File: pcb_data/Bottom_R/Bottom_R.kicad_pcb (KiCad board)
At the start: 2 copper layers, 186.9 x 96.4 mm, 103 parts, among them J1 Conn_01x02, U1 XIAO-nRF52840

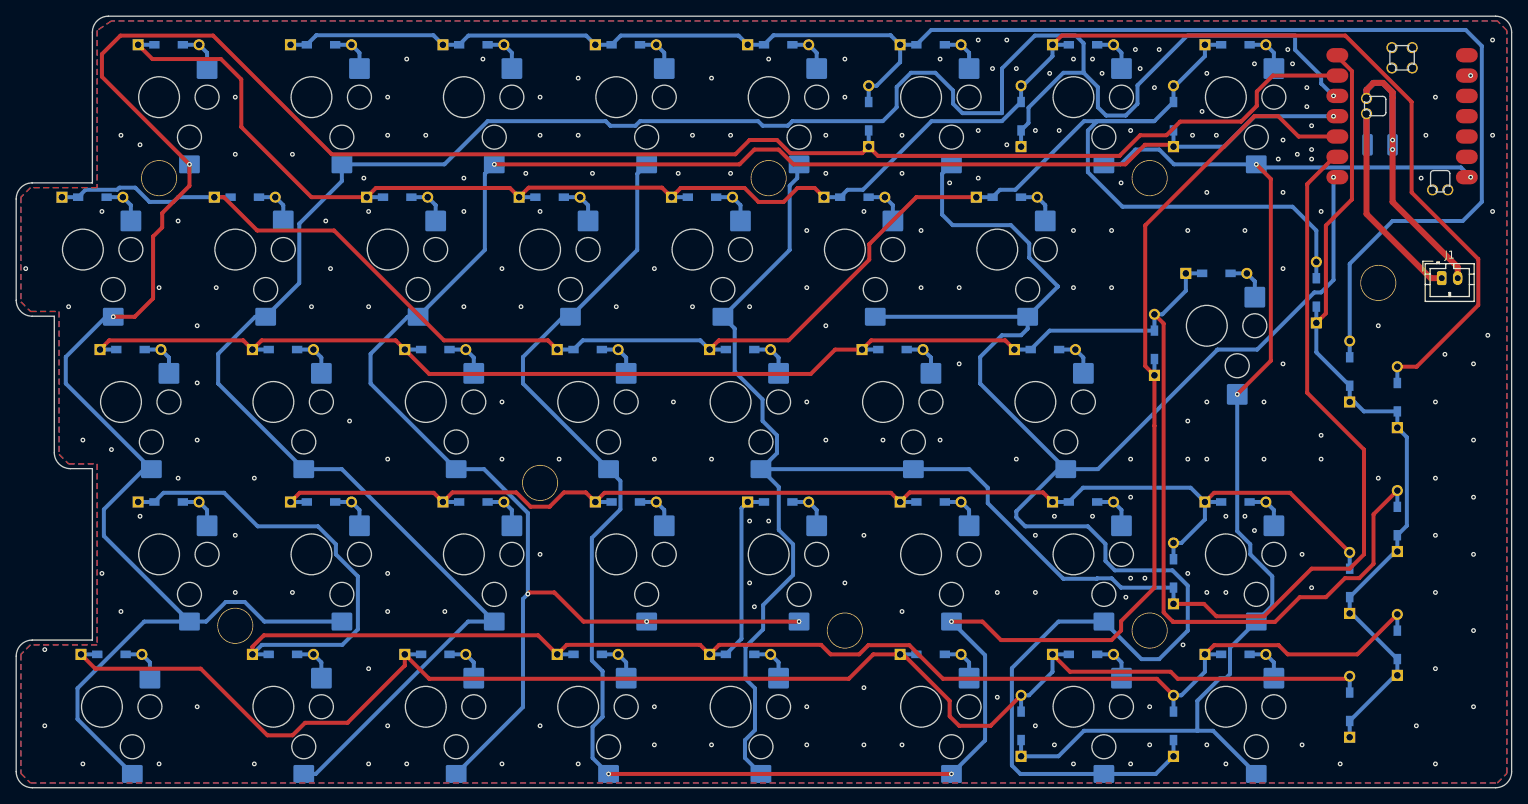
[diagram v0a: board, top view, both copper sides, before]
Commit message: remove unnecessary footprint
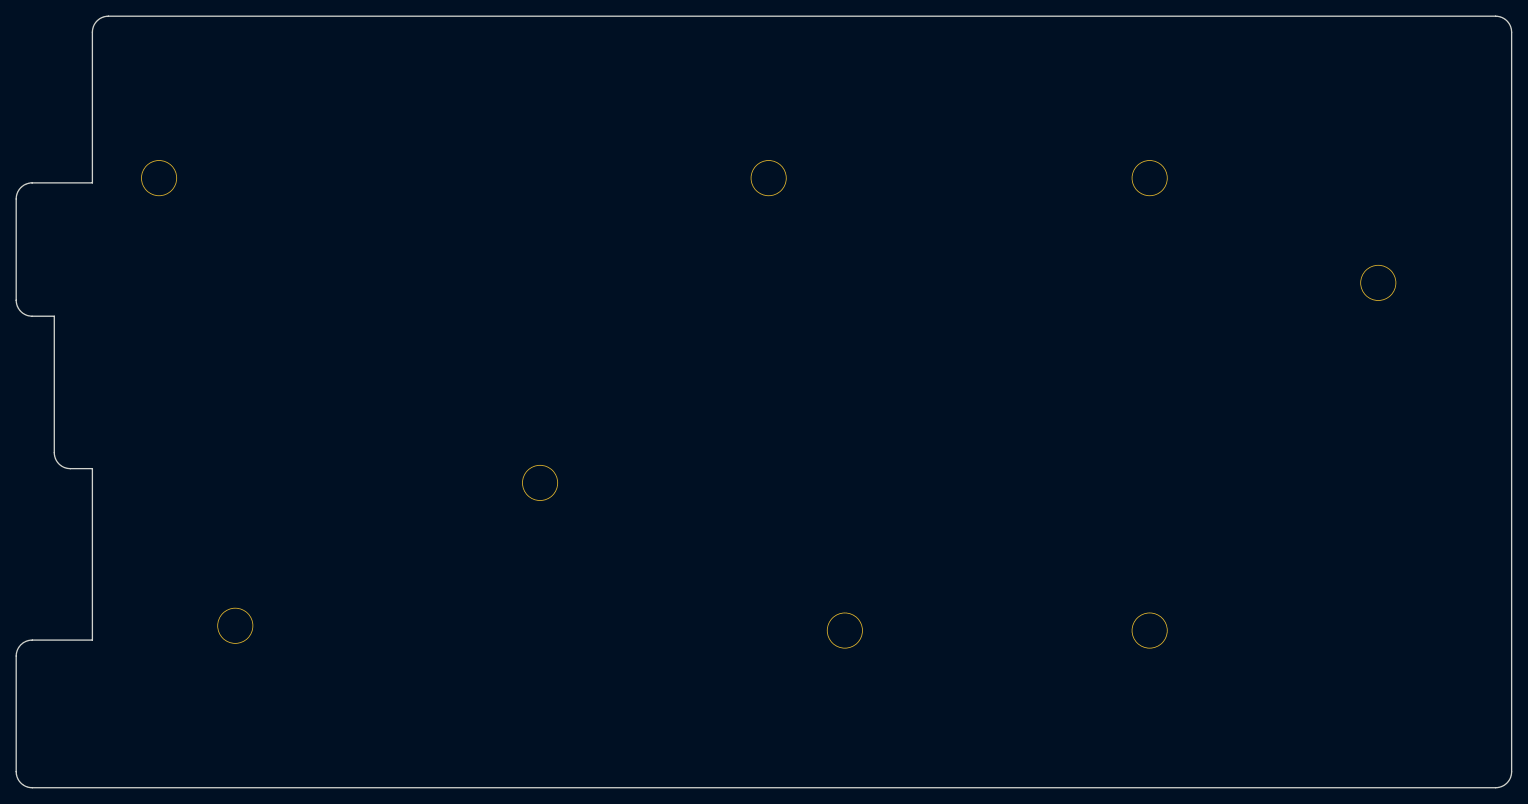
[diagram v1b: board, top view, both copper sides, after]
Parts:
- removed C1: GRM32EC81C476KE15L, Capacitor_SMD:C_1210_3225Metric_Pad1.33x2.70mm_HandSolder
- removed D0-10, D0-11, D0-12, D0-13, D0-8, D0-9, D1-10, D1-11, D1-12, D1-7, D1-9, D2-10, D2-11, D2-12, D2-13, D2-7, D2-8, D3-11, D3-12, D3-13, D3-7, D3-8, D3-9, D4-10, D4-12, D4-7, D4-8, D4-9, D5-10, D5-11, D5-13, D5-7, D5-8, D5-9, D6-10, D6-11, D6-12, D6-8, D6-9, DI10, DI11, DI12, DI13, DI7, DI8, DI9, DS10, DS11, DS12, DS13, DS7, DS8, DS9: 1N4148W, kbd_Parts:Diode_TH_SMD
- removed J1: Conn_01x02, Connector_JST:JST_PH_B2B-PH-K_1x02_P2.00mm_Vertical
- removed RC0-10, RC0-11, RC0-12, RC0-8, RC0-9, RC1-10, RC1-11, RC1-12, RC1-7, RC1-9, RC2-10, RC2-11, RC2-12, RC2-13, RC2-7, RC2-8, RC3-11, RC3-12, RC3-13, RC3-7, RC3-8, RC3-9, RC4-10, RC4-12, RC4-7, RC4-8, RC4-9, RC5-10, RC5-11, RC5-13, RC5-7, RC5-8, RC5-9, RC6-11, RC6-12, RC6-8, RC6-9: SW_Push, custom-library:Kailh-PG1353-Hotswap-R-1U
- removed RC0-13: SW_Push, custom-library:Kailh-PG1353-Hotswap-R-1.25U
- removed RC6-10: SW_Push, custom-library:Kailh-PG1353-Hotswap-ISOEnter-R
- removed U1: XIAO-nRF52840, mcu:xiao-ble-smd-cutout
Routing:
- net IO 7: track 318.6 -> 0.00 mm, vias 2 -> 0
- net IO 8: track 286.5 -> 0.00 mm, vias 1 -> 0
- net IO 10: track 264.8 -> 0.00 mm, vias 3 -> 0
- net Net-(D0-12-K): track 245.6 -> 0.00 mm
- net IO 9: track 243.9 -> 0.00 mm, vias 5 -> 0
- net Net-(D0-8-K): track 243.5 -> 0.00 mm
- net IO 12: track 238.5 -> 0.00 mm, vias 1 -> 0
- net Net-(D0-10-K): track 237.6 -> 0.00 mm
- net IO 11: track 232.4 -> 0.00 mm
- net Net-(D0-9-K): track 229.8 -> 0.00 mm
- net Net-(D1-7-K): track 214.6 -> 0.00 mm
- net Net-(D0-13-K): track 193.7 -> 0.00 mm
- net Net-(D0-11-K): track 164.4 -> 0.00 mm
- net IO 13: track 162.5 -> 0.00 mm, vias 3 -> 0
- net INTR_R: track 106.3 -> 0.00 mm
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- removed copper zone on B.Cu, net GND
- removed copper zone on F.Cu, net GND

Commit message: fix hole footprint and number
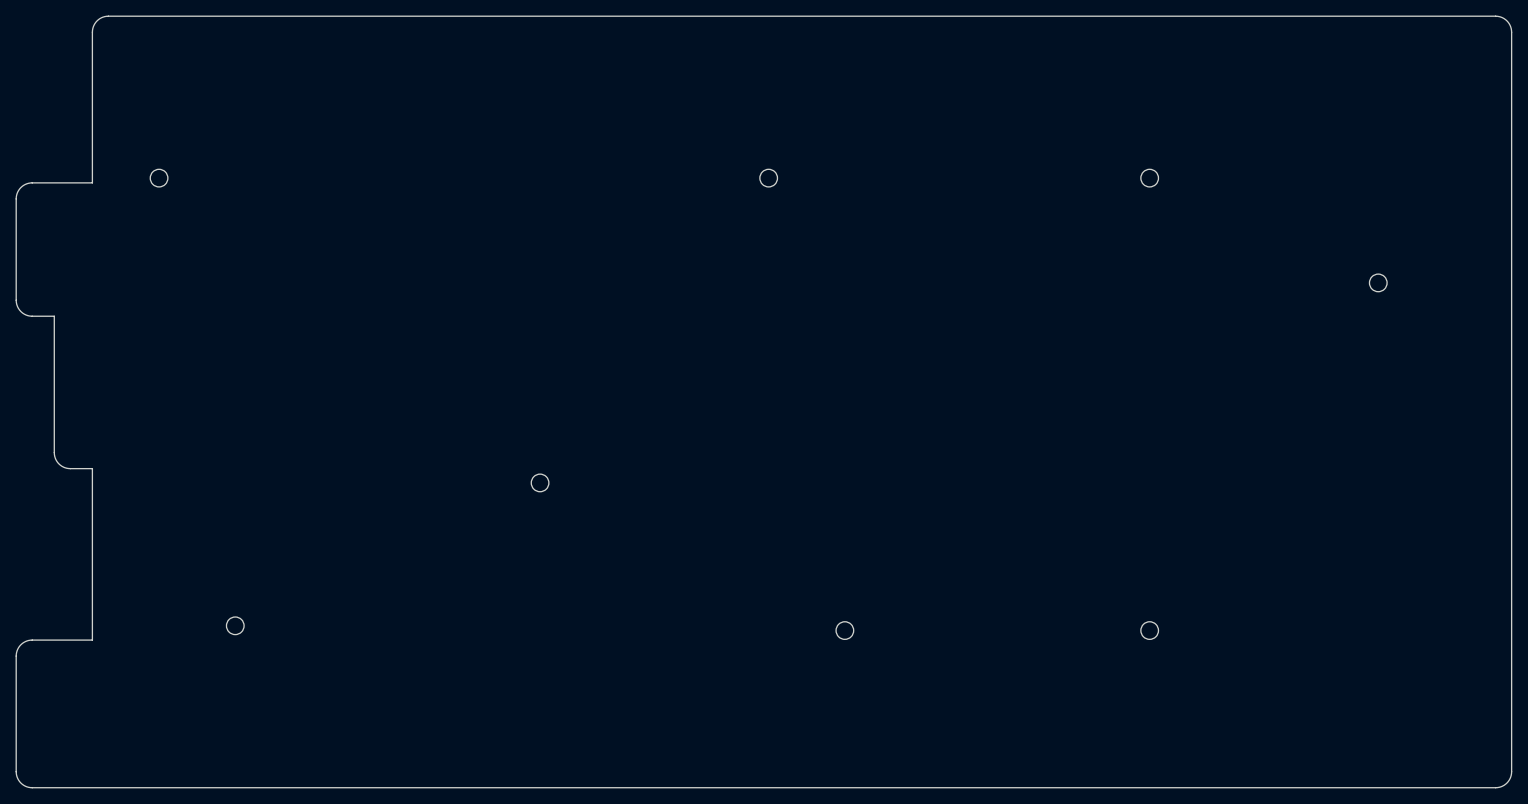
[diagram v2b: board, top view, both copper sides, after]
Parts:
- H1, H2, H3, H4, H5, H6: footprint kbd_Hole:m2_Spacer_Hole -> kbd_Hole:m2_Screw_Hole
- H7: renamed from H8; footprint kbd_Hole:m2_Spacer_Hole -> kbd_Hole:m2_Screw_Hole
- H8: renamed from H7; footprint kbd_Hole:m2_Spacer_Hole -> kbd_Hole:m2_Screw_Hole
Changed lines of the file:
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@@
 	)
 	(net 0 "")
-	(footprint "kbd_Hole:m2_Spacer_Hole"
+	(footprint "kbd_Hole:m2_Screw_Hole"
 		(layer "F.Cu")
 		(at 207.168924 67.270369)
@@
 			)
 		)
-		(property "Datasheet" "~"
-			(at 0 0 0)
-			(layer "F.Fab")
-			(hide yes)
-			(effects
-				(font
-					(size 1.27 1.27)
-					(thickness 0.15)
-				)
-			)
-		)
-		(property "Description" "Mounting Hole without connection"
+		(property "Datasheet" ""
+			(at 0 0 0)
+			(layer "F.Fab")
+			(hide yes)
+			(effects
+				(font
+					(size 1.27 1.27)
+					(thickness 0.15)
+				)
+			)
+		)
+		(property "Description" ""
 			(at 0 0 0)
 			(layer "F.Fab")
@@
 		(fp_circle
 			(center 0 0)
-			(end 2.3 0)
+			(end 2.45 0)
 			(stroke
 				(width 0.05)
@@
 		(pad "" np_thru_hole circle
 			(at 0 0)
-			(size 4.5 4.5)
-			(drill 4.3)
+			(size 2.2 2.2)
+			(drill 2.2)
 			(layers "*.Cu" "*.Mask")
 		)
 		(embedded_fonts no)
 	)
-	(footprint "kbd_Hole:m2_Spacer_Hole"
+	(footprint "kbd_Hole:m2_Screw_Hole"
 		(layer "F.Cu")
 		(at 207.168924 123.825104)
@@
 			)
 		)
-		(property "Datasheet" "~"
-			(at 0 0 0)
-			(layer "F.Fab")
-			(hide yes)
-			(effects
-				(font
-					(size 1.27 1.27)
-					(thickness 0.15)
-				)
-			)
-		)
-		(property "Description" "Mounting Hole without connection"
+		(property "Datasheet" ""
+			(at 0 0 0)
+			(layer "F.Fab")
+			(hide yes)
+			(effects
+				(font
+					(size 1.27 1.27)
+					(thickness 0.15)
+				)
+			)
+		)
+		(property "Description" ""
 			(at 0 0 0)
 			(layer "F.Fab")
@@
 		(fp_circle
 			(center 0 0)
-			(end 2.3 0)
+			(end 2.45 0)
 			(stroke
 				(width 0.05)
@@
 		(pad "" np_thru_hole circle
 			(at 0 0)
-			(size 4.5 4.5)
-			(drill 4.3)
+			(size 2.2 2.2)
+			(drill 2.2)
 			(layers "*.Cu" "*.Mask")
 		)
 		(embedded_fonts no)
 	)
-	(footprint "kbd_Hole:m2_Spacer_Hole"
+	(footprint "kbd_Hole:m2_Screw_Hole"
 		(layer "F.Cu")
 		(at 235.743948 80.367255)
 		(descr "Mounting Hole 2.2mm, no annular, M2")
 		(tags "mounting hole 2.2mm no annular m2")
-		(property "Reference" "H7"
+		(property "Reference" "H8"
 			(at 0 -3.2 0)
 			(layer "F.Fab")
@@
 			)
 		)
-		(property "Datasheet" "~"
-			(at 0 0 0)
-			(layer "F.Fab")
-			(hide yes)
-			(effects
-				(font
-					(size 1.27 1.27)
-					(thickness 0.15)
-				)
-			)
-		)
-		(property "Description" "Mounting Hole without connection"
+		(property "Datasheet" ""
+			(at 0 0 0)
+			(layer "F.Fab")
+			(hide yes)
+			(effects
+				(font
+					(size 1.27 1.27)
+					(thickness 0.15)
+				)
+			)
+		)
+		(property "Description" ""
 			(at 0 0 0)
 			(layer "F.Fab")
@@
 		(fp_circle
 			(center 0 0)
-			(end 2.3 0)
+			(end 2.45 0)
 			(stroke
 				(width 0.05)
@@
 		(pad "" np_thru_hole circle
 			(at 0 0)
-			(size 4.5 4.5)
-			(drill 4.3)
+			(size 2.2 2.2)
+			(drill 2.2)
 			(layers "*.Cu" "*.Mask")
 		)
 		(embedded_fonts no)
 	)
-	(footprint "kbd_Hole:m2_Spacer_Hole"
+	(footprint "kbd_Hole:m2_Screw_Hole"
 		(layer "F.Cu")
 		(at 130.96886 105.370401)
 		(descr "Mounting Hole 2.2mm, no annular, M2")
 		(tags "mounting hole 2.2mm no annular m2")
-		(property "Reference" "H8"
+		(property "Reference" "H7"
 			(at 0 -3.2 0)
 			(layer "F.Fab")
@@
 			)
 		)
-		(property "Datasheet" "~"
-			(at 0 0 0)
-			(layer "F.Fab")
-			(hide yes)
-			(effects
-				(font
-					(size 1.27 1.27)
-					(thickness 0.15)
-				)
-			)
-		)
-		(property "Description" "Mounting Hole without connection"
+		(property "Datasheet" ""
+			(at 0 0 0)
+			(layer "F.Fab")
+			(hide yes)
+			(effects
+				(font
+					(size 1.27 1.27)
+					(thickness 0.15)
+				)
+			)
+		)
+		(property "Description" ""
 			(at 0 0 0)
 			(layer "F.Fab")
@@
 		(fp_circle
 			(center 0 0)
-			(end 2.3 0)
+			(end 2.45 0)
 			(stroke
 				(width 0.05)
@@
 		(pad "" np_thru_hole circle
 			(at 0 0)
-			(size 4.5 4.5)
-			(drill 4.3)
+			(size 2.2 2.2)
+			(drill 2.2)
 			(layers "*.Cu" "*.Mask")
 		)
 		(embedded_fonts no)
 	)
-	(footprint "kbd_Hole:m2_Spacer_Hole"
+	(footprint "kbd_Hole:m2_Screw_Hole"
 		(layer "F.Cu")
 		(at 83.34382 67.270369)
@@
 			)
 		)
-		(property "Datasheet" "~"
-			(at 0 0 0)
-			(layer "F.Fab")
-			(hide yes)
-			(effects
-				(font
-					(size 1.27 1.27)
-					(thickness 0.15)
-				)
-			)
-		)
-		(property "Description" "Mounting Hole without connection"
+		(property "Datasheet" ""
+			(at 0 0 0)
+			(layer "F.Fab")
+			(hide yes)
+			(effects
+				(font
+					(size 1.27 1.27)
+					(thickness 0.15)
+				)
+			)
+		)
+		(property "Description" ""
 			(at 0 0 0)
 			(layer "F.Fab")
@@
 		(fp_circle
 			(center 0 0)
-			(end 2.3 0)
+			(end 2.45 0)
 			(stroke
 				(width 0.05)
@@
 		(pad "" np_thru_hole circle
 			(at 0 0)
-			(size 4.5 4.5)
-			(drill 4.3)
+			(size 2.2 2.2)
+			(drill 2.2)
 			(layers "*.Cu" "*.Mask")
 		)
 		(embedded_fonts no)
 	)
-	(footprint "kbd_Hole:m2_Spacer_Hole"
+	(footprint "kbd_Hole:m2_Screw_Hole"
 		(layer "F.Cu")
 		(at 159.543884 67.270369)
@@
 			)
 		)
-		(property "Datasheet" "~"
-			(at 0 0 0)
-			(layer "F.Fab")
-			(hide yes)
-			(effects
-				(font
-					(size 1.27 1.27)
-					(thickness 0.15)
-				)
-			)
-		)
-		(property "Description" "Mounting Hole without connection"
+		(property "Datasheet" ""
+			(at 0 0 0)
+			(layer "F.Fab")
+			(hide yes)
+			(effects
+				(font
+					(size 1.27 1.27)
+					(thickness 0.15)
+				)
+			)
+		)
+		(property "Description" ""
 			(at 0 0 0)
 			(layer "F.Fab")
@@
 		(fp_circle
 			(center 0 0)
-			(end 2.3 0)
+			(end 2.45 0)
 			(stroke
 				(width 0.05)
@@
 		(pad "" np_thru_hole circle
 			(at 0 0)
-			(size 4.5 4.5)
-			(drill 4.3)
+			(size 2.2 2.2)
+			(drill 2.2)
 			(layers "*.Cu" "*.Mask")
 		)
 		(embedded_fonts no)
 	)
-	(footprint "kbd_Hole:m2_Spacer_Hole"
+	(footprint "kbd_Hole:m2_Screw_Hole"
 		(layer "F.Cu")
 		(at 92.868828 123.229791)
@@
 			)
 		)
-		(property "Datasheet" "~"
-			(at 0 0 0)
-			(layer "F.Fab")
-			(hide yes)
-			(effects
-				(font
-					(size 1.27 1.27)
-					(thickness 0.15)
-				)
-			)
-		)
-		(property "Description" "Mounting Hole without connection"
+		(property "Datasheet" ""
+			(at 0 0 0)
+			(layer "F.Fab")
+			(hide yes)
+			(effects
+				(font
+					(size 1.27 1.27)
+					(thickness 0.15)
+				)
+			)
+		)
+		(property "Description" ""
 			(at 0 0 0)
 			(layer "F.Fab")
@@
 		(fp_circle
 			(center 0 0)
-			(end 2.3 0)
+			(end 2.45 0)
 			(stroke
 				(width 0.05)
@@
 		(pad "" np_thru_hole circle
 			(at 0 0)
-			(size 4.5 4.5)
-			(drill 4.3)
+			(size 2.2 2.2)
+			(drill 2.2)
 			(layers "*.Cu" "*.Mask")
 		)
 		(embedded_fonts no)
 	)
-	(footprint "kbd_Hole:m2_Spacer_Hole"
+	(footprint "kbd_Hole:m2_Screw_Hole"
 		(layer "F.Cu")
 		(at 169.068892 123.825104)
@@
 			)
 		)
-		(property "Datasheet" "~"
-			(at 0 0 0)
-			(layer "F.Fab")
-			(hide yes)
-			(effects
-				(font
-					(size 1.27 1.27)
-					(thickness 0.15)
-				)
-			)
-		)
-		(property "Description" "Mounting Hole without connection"
+		(property "Datasheet" ""
+			(at 0 0 0)
+			(layer "F.Fab")
+			(hide yes)
+			(effects
+				(font
+					(size 1.27 1.27)
+					(thickness 0.15)
+				)
+			)
+		)
+		(property "Description" ""
 			(at 0 0 0)
 			(layer "F.Fab")
@@
 		(fp_circle
 			(center 0 0)
-			(end 2.3 0)
+			(end 2.45 0)
 			(stroke
 				(width 0.05)
@@
 		(pad "" np_thru_hole circle
 			(at 0 0)
-			(size 4.5 4.5)
-			(drill 4.3)
+			(size 2.2 2.2)
+			(drill 2.2)
 			(layers "*.Cu" "*.Mask")
 		)
